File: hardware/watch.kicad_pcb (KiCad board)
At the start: 4 copper layers, 33 x 34 mm, 45 parts, among them J1 Conn_01x02_Male, J2 Conn_01x03_Male, J3 Conn_01x01_Male, J4 Conn_01x03_Male, J5 Conn_01x01_Male, SW1 SW_Push, SW2 SW_Push, U1 KCSA02-105, U10 STP08DP05, U11 KCSA02-105, U12 STP08DP05, U13 KCSA02-105, U2 KCSA02-105, U3 STP08DP05, U4 STP08DP05, U5 STM32L011F4Px, U6 TLV70033_SOT23-5, U7 MCP73831-2-OT, U8 LM66100, U9 LM66100, Y1 32kHz

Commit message: working on hardware rev3
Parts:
- removed C1, C16, C5: 100nF, Capacitor_SMD:C_0603_1608Metric_Pad1.05x0.95mm_HandSolder
- removed J3, J5: Conn_01x01_Male, Connector_PinHeader_2.54mm:PinHeader_1x01_P2.54mm_Vertical
- removed J4: Conn_01x03_Male, Connector_PinHeader_2.54mm:PinHeader_1x03_P2.54mm_Vertical
- added R9: 2k, Resistor_SMD:R_0603_1608Metric_Pad1.05x0.95mm_HandSolder, F.Cu at (169.0, 89.8)
- BT1, C10, C14, C15, C3, C4, C6, C7, C8, C9, R3, R6, R7, R8, U5, U6, U7, Y1: moved to F.Cu
- J1: value Conn_01x02_Male -> USB_C_Receptacle_USB2.0; footprint Connector_PinHeader_2.54mm:PinHeader_1x02_P2.54mm_Vertical -> Connector_USB:USB_C_Receptacle_Palconn_UTC16-G; moved to F.Cu
- J2: value Conn_01x03_Male -> Conn_01x04_Male; footprint Connector_PinHeader_2.54mm:PinHeader_1x03_P2.54mm_Vertical -> Connector_PinHeader_2.54mm:PinHeader_1x04_P2.54mm_Vertical; moved to F.Cu
- R2: value 2k -> 10k
- U10, U4: moved to B.Cu
- U12: value STP08DP05 -> TCPP01-M12; footprint Package_SO:TSSOP-16_4.4x5mm_P0.65mm -> Package_DFN_QFN:QFN-12-1EP_3x3mm_P0.51mm_EP1.45x1.45mm
- U3: value STP08DP05 -> TPS2115A-Q1; footprint Package_SO:TSSOP-16_4.4x5mm_P0.65mm -> watch:TSSOP-8_3x6.4_P0.65mm
- U8, U9: value LM66100 -> STP08DP05; footprint lm66100:LM66100DCKT -> Package_SO:TSSOP-16_4.4x5mm_P0.65mm
- moved R4 50.5 mm to (169.0, 87.3), turned to 0 degrees
- moved BT1 38.3 mm to (190.5, 60.9), turned to 0 degrees
- moved J2 35.1 mm to (144.0, 42.9)
- moved R5 33.7 mm to (177.8, 80.7), turned to 0 degrees
- moved U12 27.1 mm to (127.5, 54.9)
- moved C10 24.6 mm to (155.4, 49.7), turned to 0 degrees
- moved C11 24.2 mm to (136.0, 75.9), turned to 0 degrees
- moved SW1 23.9 mm to (136.0, 72.9)
- moved R8 23.1 mm to (144.9, 47.9), turned to 0 degrees
- moved C4 23.0 mm to (164.5, 49.4)
- moved U1 22.5 mm to (158.3, 62.9)
- moved U13 22.5 mm to (135.8, 62.9)
- moved U10 21.2 mm to (158.3, 62.9), turned to -90 degrees
- moved C6 19.6 mm to (139.0, 49.4), turned to 180 degrees
- moved R2 19.5 mm to (157.5, 54.9), turned to 0 degrees
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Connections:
- U1 pad 1: /S1_E -> /S2_E
- U1 pad 10: /S1_G -> /S2_G
- U1 pad 2: /S1_D -> /S2_D
- U1 pad 4: /S1_C -> /S2_C
- U1 pad 5: /S1_DP -> /S2_DP
- U1 pad 6: /S1_B -> /S2_B
- U1 pad 7: /S1_A -> /S2_A
- U1 pad 9: /S1_F -> /S2_F
- U10 pad 10: /S2_G -> Net-(U10-Pad10)
- U10 pad 11: /S2_A -> Net-(U10-Pad11)
- U10 pad 12: /S2_B -> Net-(U10-Pad12)
- U10 pad 15: Net-(R4-Pad1) -> Net-(R9-Pad1)
- U10 pad 5: /S1_G -> Net-(U10-Pad5)
- U10 pad 6: /S1_F -> Net-(U10-Pad6)
- U10 pad 7: /S1_B -> Net-(U10-Pad7)
- U10 pad 8: /S1_A -> Net-(U10-Pad8)
- U10 pad 9: /S2_F -> Net-(U10-Pad9)
- U11 pad 1: /S3_E -> /S2_E
- U11 pad 10: /S3_G -> /S2_G
- U11 pad 2: /S3_D -> /S2_D
- U11 pad 4: /S3_C -> /S2_C
- U11 pad 5: /S3_DP -> /S2_DP
- U11 pad 6: /S3_B -> /S2_B
- U11 pad 7: /S3_A -> /S2_A
- U11 pad 9: /S3_F -> /S2_F
- U12 pad 1: GND -> Net-(U12-Pad1)
- U12 pad 10: /S4_G -> Net-(U12-Pad10)
- U12 pad 11: /S4_A -> Net-(U12-Pad11)
- U12 pad 12: /S4_B -> Net-(U12-Pad12)
- U12 pad 13: /OE -> Net-(U12-Pad13)
- U12 pad 2: Net-(U10-Pad14) -> Net-(U12-Pad2)
- U12 pad 3: /CLK -> Net-(U12-Pad3)
- U12 pad 4: /LE -> Net-(U12-Pad4)
- U12 pad 5: /S3_G -> Net-(U12-Pad5)
- U12 pad 6: /S3_F -> Net-(U12-Pad6)
- U12 pad 7: /S3_B -> Net-(U12-Pad7)
- U12 pad 8: /S3_A -> Net-(U12-Pad8)
- U12 pad 9: /S4_F -> Net-(U12-Pad9)
- U13 pad 1: /S4_E -> /S2_E
- U13 pad 10: /S4_G -> /S2_G
- U13 pad 2: /S4_D -> /S2_D
- U13 pad 4: /S4_C -> /S2_C
- U13 pad 5: /S4_DP -> /S2_DP
- U13 pad 6: /S4_B -> /S2_B
- U13 pad 7: /S4_A -> /S2_A
- U13 pad 9: /S4_F -> /S2_F
- U3 pad 1: GND -> Net-(U3-Pad1)
- U3 pad 2: Net-(U3-Pad2) -> GND
- U3 pad 3: /CLK -> Net-(U3-Pad3)
- U3 pad 4: /LE -> Net-(R2-Pad1)
- U3 pad 5: /S4_DP -> +5V
- U3 pad 6: /S4_C -> VCC
- U3 pad 7: /S4_E -> +BATT
- U3 pad 8: /S4_D -> GND
- U4 pad 14: Net-(U3-Pad2) -> Net-(U4-Pad14)
- U5 pad 8: /TX -> Net-(U5-Pad8)
- U5 pad 9: /RX -> Net-(U5-Pad9)
- U8 pad 1: +BATT -> GND
- U8 pad 2: GND -> Net-(U4-Pad14)
- U8 pad 3: +5V -> /CLK
- U8 pad 4: (no net) -> /LE
- U8 pad 5: GND -> Net-(U8-Pad5)
- U8 pad 6: VCC -> Net-(U8-Pad6)
- U9 pad 1: +5V -> GND
- U9 pad 2: GND -> Net-(U8-Pad14)
- U9 pad 3: +BATT -> /CLK
- U9 pad 4: (no net) -> /LE
- U9 pad 5: GND -> Net-(U9-Pad5)
- U9 pad 6: VCC -> Net-(U9-Pad6)
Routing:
- net GND: track 85.1 -> 0.00 mm, vias 13 -> 0
- net /OE: track 74.3 -> 0.00 mm, vias 4 -> 0
- net /CLK: track 72.9 -> 0.00 mm, vias 4 -> 0
- net /LE: track 69.2 -> 0.00 mm, vias 4 -> 0
- net +3V3: track 61.6 -> 0.00 mm, vias 7 -> 0
- net Net-(U10-Pad2): track 51.4 -> 0.00 mm, vias 2 -> 0
- net /RX: track 46.1 -> 0.00 mm, vias 1 -> 0
- net /ADC: track 44.1 -> 0.00 mm
- net +BATT: track 42.9 -> 0.00 mm, vias 2 -> 0
- net VCC: track 40.8 -> 0.00 mm, vias 2 -> 0
- net /TX: track 39.9 -> 0.00 mm, vias 1 -> 0
- net /SW1: track 31.8 -> 0.00 mm, vias 1 -> 0
- net +5V: track 29.2 -> 0.00 mm
- net /MDI: track 26.2 -> 0.00 mm, vias 1 -> 0
- net /NRST: track 24.2 -> 0.00 mm
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- removed copper zone on B.Cu, net +3V3
- removed copper zone on In1.Cu, net +3V3
- removed copper zone on B.Cu, net +5V
- removed copper zone on B.Cu, net +BATT
- removed copper zone on B.Cu, net GND
- removed copper zone on In2.Cu, net GND
- removed copper zone on B.Cu, net VCC
- removed copper zone on F.Cu, net VCC
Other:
- board size 33 x 34 mm -> 48 x 34 mm
- net class Default removed
- board text removed: "BAT"
- board text removed: "SWD"
- board text removed: "UART"

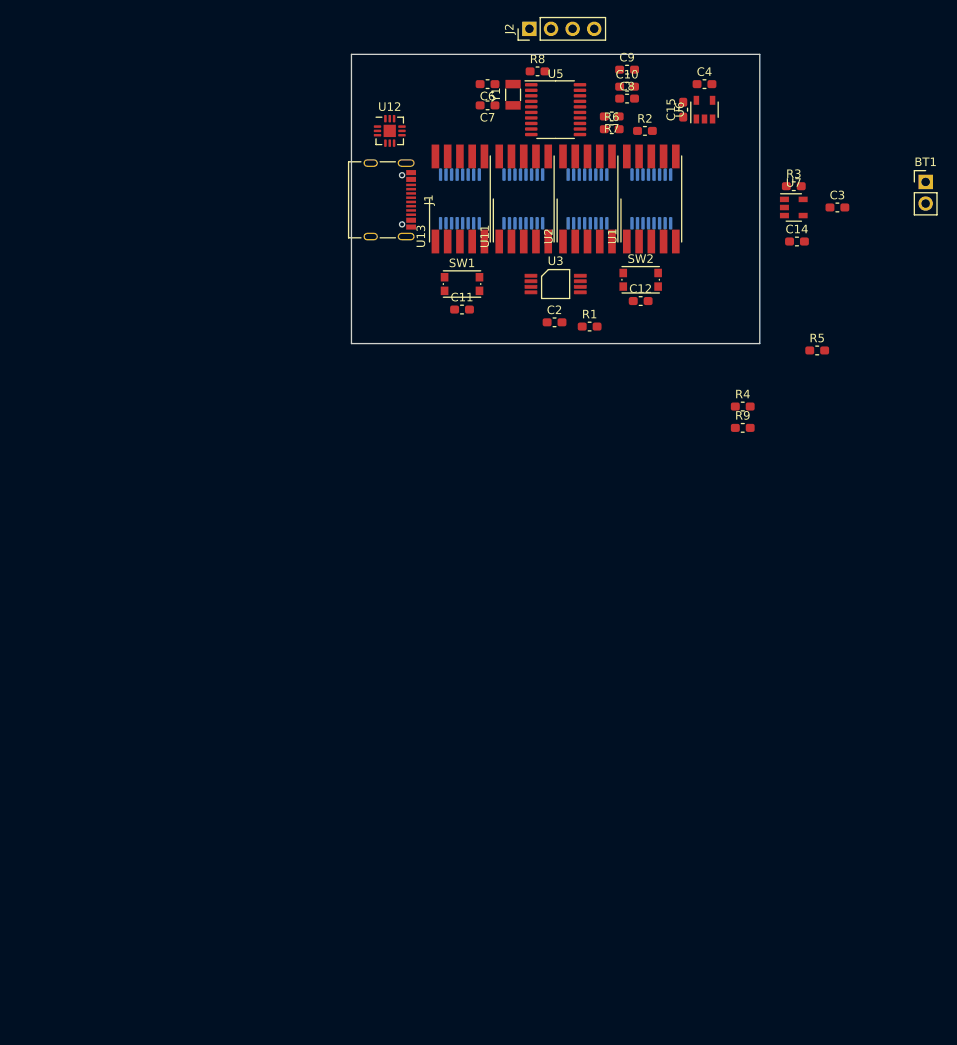
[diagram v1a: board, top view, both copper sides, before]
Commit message: schematic should be done, pcb is next
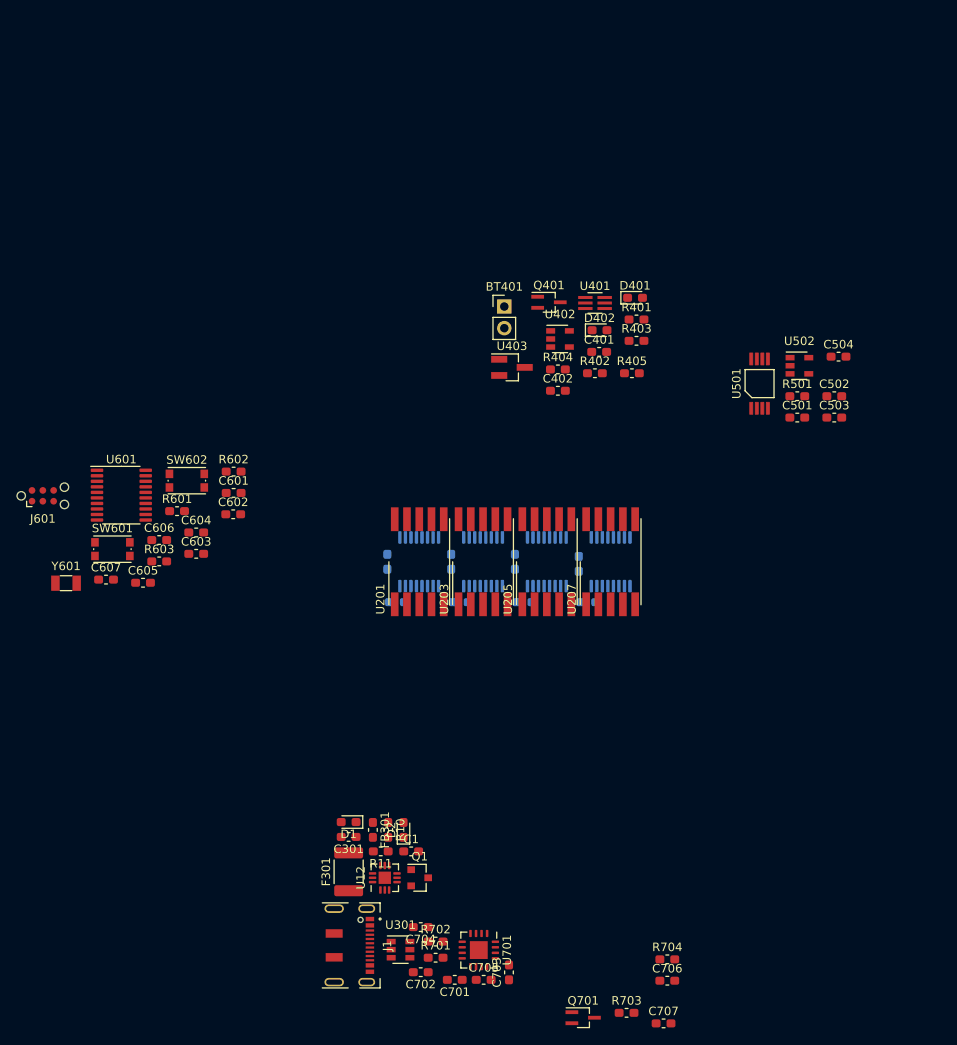
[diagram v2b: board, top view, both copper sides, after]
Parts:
- removed BT1: Battery_Cell, Connector_PinHeader_2.54mm:PinHeader_1x02_P2.54mm_Vertical
- removed C10, C11, C12, C2, C9: 100nF, Capacitor_SMD:C_0603_1608Metric_Pad1.05x0.95mm_HandSolder
- removed C14, C3, C8: 10uF, Capacitor_SMD:C_0603_1608Metric_Pad1.05x0.95mm_HandSolder
- removed C15, C4: 1uF, Capacitor_SMD:C_0603_1608Metric_Pad1.05x0.95mm_HandSolder
- removed C6, C7: 12pF, Capacitor_SMD:C_0603_1608Metric_Pad1.05x0.95mm_HandSolder
- removed J2: Conn_01x04_Male, Connector_PinHeader_2.54mm:PinHeader_1x04_P2.54mm_Vertical
- removed R1, R4, R5, R9: 2k, Resistor_SMD:R_0603_1608Metric_Pad1.05x0.95mm_HandSolder
- removed R2: 10k, Resistor_SMD:R_0603_1608Metric_Pad1.05x0.95mm_HandSolder
- removed R3: 3k9, Resistor_SMD:R_0603_1608Metric_Pad1.05x0.95mm_HandSolder
- removed R6, R7: 47k, Resistor_SMD:R_0603_1608Metric_Pad1.05x0.95mm_HandSolder
- removed R8: 100k, Resistor_SMD:R_0603_1608Metric_Pad1.05x0.95mm_HandSolder
- removed SW1, SW2: SW_Push, Button_Switch_SMD:SW_Push_1P1T_NO_CK_KMR2
- removed U1, U11, U13, U2: KCSA02-105, Display_7Segment:KCSC02-105
- removed U10, U4, U8, U9: STP08DP05, Package_SO:TSSOP-16_4.4x5mm_P0.65mm
- removed U3: TPS2115A-Q1, watch:TSSOP-8_3x6.4_P0.65mm
- removed U5: STM32L011F4Px, Package_SO:TSSOP-20_4.4x6.5mm_P0.65mm
- removed U6: TLV70033_SOT23-5, Package_TO_SOT_SMD:SOT-23-5
- removed U7: MCP73831-2-OT, Package_TO_SOT_SMD:SOT-23-5
- removed Y1: 32kHz, Crystal:Crystal_SMD_3215-2Pin_3.2x1.5mm
- added BT401: Battery_Cell, Connector_PinHeader_2.54mm:PinHeader_1x02_P2.54mm_Vertical, F.Cu at (141.0, 75.5)
- added C1: 100n, Capacitor_SMD:C_0603_1608Metric_Pad1.05x0.95mm_HandSolder, F.Cu at (130.1, 139.6)
- added C201: 100n, Capacitor_SMD:C_0603_1608Metric_Pad1.05x0.95mm_HandSolder, B.Cu at (127.2, 105.5)
- added C202: 100n, Capacitor_SMD:C_0603_1608Metric_Pad1.05x0.95mm_HandSolder, B.Cu at (134.8, 105.5)
- added C203: 100n, Capacitor_SMD:C_0603_1608Metric_Pad1.05x0.95mm_HandSolder, B.Cu at (142.2, 105.5)
- added C204: 100n, Capacitor_SMD:C_0603_1608Metric_Pad1.05x0.95mm_HandSolder, B.Cu at (149.8, 105.8)
- added C301: 10n, Capacitor_SMD:C_0603_1608Metric_Pad1.05x0.95mm_HandSolder, F.Cu at (122.7, 137.8)
- added C401: 10u, Capacitor_SMD:C_0603_1608Metric_Pad1.05x0.95mm_HandSolder, F.Cu at (152.2, 80.8)
- added C402: 10u, Capacitor_SMD:C_0603_1608Metric_Pad1.05x0.95mm_HandSolder, F.Cu at (147.3, 85.4)
- added C501: 100n, Capacitor_SMD:C_0603_1608Metric_Pad1.05x0.95mm_HandSolder, F.Cu at (175.4, 88.5)
- added C502: 100n, Capacitor_SMD:C_0603_1608Metric_Pad1.05x0.95mm_HandSolder, F.Cu at (179.8, 86.0)
- added C503: 1u, Capacitor_SMD:C_0603_1608Metric_Pad1.05x0.95mm_HandSolder, F.Cu at (179.8, 88.5)
- added C504: 1u, Capacitor_SMD:C_0603_1608Metric_Pad1.05x0.95mm_HandSolder, F.Cu at (180.3, 81.4)
- added C601: 12p, Capacitor_SMD:C_0603_1608Metric_Pad1.05x0.95mm_HandSolder, F.Cu at (109.2, 97.4)
- added C602: 12p, Capacitor_SMD:C_0603_1608Metric_Pad1.05x0.95mm_HandSolder, F.Cu at (109.1, 99.9)
- added C603: 100n, Capacitor_SMD:C_0603_1608Metric_Pad1.05x0.95mm_HandSolder, F.Cu at (104.8, 104.6)
- added C604: 100n, Capacitor_SMD:C_0603_1608Metric_Pad1.05x0.95mm_HandSolder, F.Cu at (104.8, 102.1)
- added C605: 10u, Capacitor_SMD:C_0603_1608Metric_Pad1.05x0.95mm_HandSolder, F.Cu at (98.5, 108.0)
- added C606: 100n, Capacitor_SMD:C_0603_1608Metric_Pad1.05x0.95mm_HandSolder, F.Cu at (100.4, 103.0)
- added C607: 100n, Capacitor_SMD:C_0603_1608Metric_Pad1.05x0.95mm_HandSolder, F.Cu at (94.2, 107.6)
- added C701: 100n, Capacitor_SMD:C_0603_1608Metric_Pad1.05x0.95mm_HandSolder, F.Cu at (135.2, 154.7)
- added C702: 47p, Capacitor_SMD:C_0603_1608Metric_Pad1.05x0.95mm_HandSolder, F.Cu at (131.2, 153.8)
- added C703: 4.7u, Capacitor_SMD:C_0603_1608Metric_Pad1.05x0.95mm_HandSolder, F.Cu at (141.6, 153.8)
- added C704: 47p, Capacitor_SMD:C_0603_1608Metric_Pad1.05x0.95mm_HandSolder, F.Cu at (131.2, 148.4)
- added C705: 100n, Capacitor_SMD:C_0603_1608Metric_Pad1.05x0.95mm_HandSolder, F.Cu at (138.6, 154.7)
- added C706: 100n, Capacitor_SMD:C_0603_1608Metric_Pad1.05x0.95mm_HandSolder, F.Cu at (160.2, 154.8)
- added C707: 100n, Capacitor_SMD:C_0603_1608Metric_Pad1.05x0.95mm_HandSolder, F.Cu at (159.7, 159.8)
- added D1: ESDA25P35-1U1M, Diode_SMD:D_0603_1608Metric_Pad1.05x0.95mm_HandSolder, F.Cu at (122.7, 136.1)
- added D2: NSR20F30NXT5G, Diode_SMD:D_0603_1608Metric_Pad1.05x0.95mm_HandSolder, F.Cu at (129.2, 137.0)
- added D401: RED, LED_SMD:LED_0603_1608Metric_Pad1.05x0.95mm_HandSolder, F.Cu at (156.4, 74.5)
- added D402: GREEN, LED_SMD:LED_0603_1608Metric_Pad1.05x0.95mm_HandSolder, F.Cu at (152.2, 78.3)
- added F301: 1812L050/60MR, Fuse:Fuse_1812_4532Metric_Pad1.30x3.40mm_HandSolder, F.Cu at (122.7, 141.9)
- added FB301: 600R@100MHz, Inductor_SMD:L_0603_1608Metric_Pad1.05x0.95mm_HandSolder, F.Cu at (125.5, 137.0)
- added J601: SWD, Connector:Tag-Connect_TC2030-IDC-NL_2x03_P1.27mm_Vertical, F.Cu at (86.8, 97.8)
- added Q1: DMN6140L, Package_TO_SOT_SMD:SOT-23, F.Cu at (131.1, 142.7)
- added Q401: DMP2110UW-7, Package_TO_SOT_SMD:SOT-323_SC-70_Handsoldering, F.Cu at (146.2, 75.0)
- added Q701: DMP2110UW-7, Package_TO_SOT_SMD:SOT-323_SC-70_Handsoldering, F.Cu at (150.3, 159.1)
- added R10: 10k, Resistor_SMD:R_0603_1608Metric_Pad1.05x0.95mm_HandSolder, F.Cu at (127.3, 137.0)
- added R11: 2k7, Resistor_SMD:R_0603_1608Metric_Pad1.05x0.95mm_HandSolder, F.Cu at (126.5, 139.6)
- added R201: 2k, Resistor_SMD:R_0603_1608Metric_Pad1.05x0.95mm_HandSolder, B.Cu at (128.4, 110.2)
- added R202: 2k, Resistor_SMD:R_0603_1608Metric_Pad1.05x0.95mm_HandSolder, B.Cu at (135.9, 110.2)
- added R203: 2k, Resistor_SMD:R_0603_1608Metric_Pad1.05x0.95mm_HandSolder, B.Cu at (143.4, 110.2)
- added R204: 2k, Resistor_SMD:R_0603_1608Metric_Pad1.05x0.95mm_HandSolder, B.Cu at (150.9, 110.2)
- added R401: 10k, Resistor_SMD:R_0603_1608Metric_Pad1.05x0.95mm_HandSolder, F.Cu at (156.5, 77.0)
- added R402: 10k, Resistor_SMD:R_0603_1608Metric_Pad1.05x0.95mm_HandSolder, F.Cu at (151.7, 83.3)
- added R403: R, Resistor_SMD:R_0603_1608Metric_Pad1.05x0.95mm_HandSolder, F.Cu at (156.5, 79.5)
- added R404: 47k, Resistor_SMD:R_0603_1608Metric_Pad1.05x0.95mm_HandSolder, F.Cu at (147.3, 82.9)
- added R405: 47k, Resistor_SMD:R_0603_1608Metric_Pad1.05x0.95mm_HandSolder, F.Cu at (156.0, 83.3)
- added R501: 10k, Resistor_SMD:R_0603_1608Metric_Pad1.05x0.95mm_HandSolder, F.Cu at (175.4, 86.0)
- added R601: R_Small, Resistor_SMD:R_0603_1608Metric_Pad1.05x0.95mm_HandSolder, F.Cu at (102.5, 99.5)
- added R602: 100k, Resistor_SMD:R_0603_1608Metric_Pad1.05x0.95mm_HandSolder, F.Cu at (109.2, 94.9)
- added R603: R_Small, Resistor_SMD:R_0603_1608Metric_Pad1.05x0.95mm_HandSolder, F.Cu at (100.4, 105.5)
- added R701: 27R, Resistor_SMD:R_0603_1608Metric_Pad1.05x0.95mm_HandSolder, F.Cu at (132.9, 152.1)
- added R702: 27R, Resistor_SMD:R_0603_1608Metric_Pad1.05x0.95mm_HandSolder, F.Cu at (132.9, 150.2)
- added R703: 100k, Resistor_SMD:R_0603_1608Metric_Pad1.05x0.95mm_HandSolder, F.Cu at (155.4, 158.5)
- added R704: 1k, Resistor_SMD:R_0603_1608Metric_Pad1.05x0.95mm_HandSolder, F.Cu at (160.2, 152.2)
- added SW601: SW_Push, Button_Switch_SMD:SW_Push_1P1T_NO_CK_KMR2, F.Cu at (94.9, 104.0)
- added SW602: SW_Push, Button_Switch_SMD:SW_Push_1P1T_NO_CK_KMR2, F.Cu at (103.7, 96.0)
- added U201: KCSA02-105, Display_7Segment:KCSC02-105, F.Cu at (131.0, 105.5)
- added U202: STP08DP05, Package_SO:TSSOP-16_4.4x5mm_P0.65mm, B.Cu at (131.0, 105.5)
- added U203: KCSA02-105, Display_7Segment:KCSC02-105, F.Cu at (138.5, 105.5)
- added U204: STP08DP05, Package_SO:TSSOP-16_4.4x5mm_P0.65mm, B.Cu at (138.5, 105.5)
- added U205: KCSA02-105, Display_7Segment:KCSC02-105, F.Cu at (146.0, 105.5)
- added U206: STP08DP05, Package_SO:TSSOP-16_4.4x5mm_P0.65mm, B.Cu at (153.5, 105.5)
- added U207: KCSA02-105, Display_7Segment:KCSC02-105, F.Cu at (153.5, 105.5)
- added U208: STP08DP05, Package_SO:TSSOP-16_4.4x5mm_P0.65mm, B.Cu at (146.0, 105.5)
- added U301: USBLC6-2SC6, Package_TO_SOT_SMD:SOT-23-6, F.Cu at (128.8, 151.1)
- added U401: LM66100, lm66100:LM66100DCKT, F.Cu at (151.7, 75.1)
- added U402: MCP73831-2-OT, Package_TO_SOT_SMD:SOT-23-5, F.Cu at (147.6, 79.3)
- added U403: TLV810E, Package_TO_SOT_SMD:SOT-23_Handsoldering, F.Cu at (141.9, 82.7)
- added U501: TPS2115A-Q1, watch:TSSOP-8_3x6.4_P0.65mm, F.Cu at (171.0, 84.6)
- added U502: TLV70033_SOT23-5, Package_TO_SOT_SMD:SOT-23-5, F.Cu at (175.7, 82.5)
- added U601: STM32L011F4Px, Package_SO:TSSOP-20_4.4x6.5mm_P0.65mm, F.Cu at (96.0, 97.7)
- added U701: FT230XQ, Package_DFN_QFN:QFN-16-1EP_4x4mm_P0.65mm_EP2.1x2.1mm, F.Cu at (138.0, 151.2)
- added Y601: 32kHz, Crystal:Crystal_SMD_3215-2Pin_3.2x1.5mm, F.Cu at (89.5, 108.0)
- J1: value USB_C_Receptacle_USB2.0 -> DX07S016JA1R1500; footprint Connector_USB:USB_C_Receptacle_Palconn_UTC16-G -> watch:DX07S016JA1R1500
- moved J1 87.9 mm to (121.0, 150.6)
- moved U12 87.8 mm to (127.0, 142.7), turned to 90 degrees
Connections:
- net Net-(J1-PadA4) renamed /USB Protection Circuits/VBUS
- J1 pad A1: Net-(J1-PadA1) -> GND
- J1 pad A12: Net-(J1-PadA1) -> GND
- J1 pad A5: Net-(J1-PadA5) -> /USB Protection Circuits/CC1
- J1 pad A6: Net-(J1-PadA6) -> /USB Protection Circuits/D+_IN
- J1 pad A7: Net-(J1-PadA7) -> /USB Protection Circuits/D-_IN
- J1 pad B1: Net-(J1-PadA1) -> GND
- J1 pad B12: Net-(J1-PadA1) -> GND
- J1 pad B5: Net-(J1-PadB5) -> /USB Protection Circuits/CC2
- J1 pad B6: Net-(J1-PadB6) -> /USB Protection Circuits/D+_IN
- J1 pad B7: Net-(J1-PadB7) -> /USB Protection Circuits/D-_IN
- J1 pad S1: Net-(J1-PadS1) -> GND
- U12 pad 1: Net-(U12-Pad1) -> GND
- U12 pad 10: Net-(U12-Pad10) -> GND
- U12 pad 11: Net-(U12-Pad11) -> GND
- U12 pad 12: Net-(U12-Pad12) -> GND
- U12 pad 13: Net-(U12-Pad13) -> GND
- U12 pad 2: Net-(U12-Pad2) -> GND
- U12 pad 3: Net-(U12-Pad3) -> GND
- U12 pad 4: Net-(U12-Pad4) -> /USB Protection Circuits/5V@500mA
- U12 pad 6: Net-(U12-Pad6) -> /USB Protection Circuits/V_BUS_CTRL
- U12 pad 7: Net-(U12-Pad7) -> /USB Protection Circuits/CC1
- U12 pad 9: Net-(U12-Pad9) -> /USB Protection Circuits/CC2
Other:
- board outline removed
- net class Default added: clearance 0.2, trace_width 0.25, via_dia 0.8, via_drill 0.4

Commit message: wip hw
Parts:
- C1, C301: footprint Capacitor_SMD:C_0603_1608Metric_Pad1.05x0.95mm_HandSolder -> Capacitor_SMD:C_0603_1608Metric; moved to B.Cu
- C201, C202, C203, C204, C501, C502, C503, C504, C601, C602, C603, C604, C606, C607, C701, C702, C704, C705, C706, C707: footprint Capacitor_SMD:C_0603_1608Metric_Pad1.05x0.95mm_HandSolder -> Capacitor_SMD:C_0603_1608Metric
- C401, C402, C605, C703: footprint Capacitor_SMD:C_0603_1608Metric_Pad1.05x0.95mm_HandSolder -> Capacitor_SMD:C_0805_2012Metric
- D1, D2: footprint Diode_SMD:D_0603_1608Metric_Pad1.05x0.95mm_HandSolder -> Diode_SMD:D_0603_1608Metric; moved to B.Cu
- D401, D402: footprint LED_SMD:LED_0603_1608Metric_Pad1.05x0.95mm_HandSolder -> LED_SMD:LED_0603_1608Metric
- F301: footprint Fuse:Fuse_1812_4532Metric_Pad1.30x3.40mm_HandSolder -> Fuse:Fuse_1812_4532Metric; moved to B.Cu
- FB301: footprint Inductor_SMD:L_0603_1608Metric_Pad1.05x0.95mm_HandSolder -> Inductor_SMD:L_0603_1608Metric; moved to B.Cu
- Q1, U12: moved to B.Cu
- Q401, Q701: footprint Package_TO_SOT_SMD:SOT-323_SC-70_Handsoldering -> Package_TO_SOT_SMD:SOT-323_SC-70
- R10, R11: footprint Resistor_SMD:R_0603_1608Metric_Pad1.05x0.95mm_HandSolder -> Resistor_SMD:R_0603_1608Metric; moved to B.Cu
- R201, R202, R203, R204, R401, R402, R403, R404, R405, R501, R601, R602, R603, R701, R702, R703, R704: footprint Resistor_SMD:R_0603_1608Metric_Pad1.05x0.95mm_HandSolder -> Resistor_SMD:R_0603_1608Metric
- U401: footprint lm66100:LM66100DCKT -> watch:Sc70-6
- U403: footprint Package_TO_SOT_SMD:SOT-23_Handsoldering -> Package_TO_SOT_SMD:SOT-23
- moved R603 58.9 mm to (159.2, 102.0)
- moved SW602 56.4 mm to (159.2, 105.7), turned to 90 degrees
- moved C604 54.4 mm to (159.2, 100.4)
- moved C607 52.1 mm to (144.2, 92.9)
- moved BT401 49.8 mm to (159.8, 121.6), turned to 180 degrees
- moved Y601 47.5 mm to (133.3, 89.7), turned to 90 degrees
- moved C605 47.0 mm to (144.3, 97.7)
- moved C707 43.7 mm to (146.7, 118.0), turned to 180 degrees
- moved D401 43.5 mm to (151.4, 117.6), turned to 90 degrees
- moved U601 42.8 mm to (138.5, 93.2)
- moved D402 42.5 mm to (151.4, 120.8), turned to 90 degrees
- moved R501 41.9 mm to (144.3, 114.1), turned to 90 degrees
- moved U402 41.7 mm to (154.1, 120.5), turned to 90 degrees
- moved R401 41.2 mm to (149.8, 117.7), turned to 90 degrees
- moved U401 40.2 mm to (155.9, 115.0), turned to 270 degrees
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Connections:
- net /USB Protection Circuits/D+_IN renamed /USB Protection Circuits/IN_D+
- net /USB Protection Circuits/D-_IN renamed /USB Protection Circuits/IN_D-
- net Net-(R701-Pad2) renamed /USB/CHIP_D+
- net Net-(R702-Pad2) renamed /USB/CHIP_D-
- D402 pad 1: GND -> Net-(D402-Pad1)
- D402 pad 2: Net-(D402-Pad2) -> /Battery Charger/STAT
- R402 pad 1: /Battery Charger/STAT -> Net-(D402-Pad1)
- R402 pad 2: Net-(D402-Pad2) -> GND
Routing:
- net GND: track 0.00 -> 190.7 mm, vias 0 -> 1
- net /Display/V_DISP: track 0.00 -> 71.4 mm, vias 0 -> 2
- net +3V3: track 0.00 -> 37.0 mm
- net /USB Protection Circuits/5V@500mA: track 0.00 -> 33.2 mm, vias 0 -> 1
- net Net-(D1-Pad1): track 0.00 -> 25.3 mm
- net /USB Protection Circuits/V_BUS_CTRL: track 0.00 -> 24.8 mm
- net /USB Protection Circuits/CC1: track 0.00 -> 21.7 mm, vias 0 -> 1
- net /USB Protection Circuits/CC2: track 0.00 -> 18.2 mm, vias 0 -> 1
- net Net-(BT401-Pad1): track 0.00 -> 15.0 mm
- net /Power Selection Circuits/5V: track 0.00 -> 13.8 mm
- net Net-(C401-Pad1): track 0.00 -> 13.4 mm
- net Net-(U202-Pad14): track 0.00 -> 12.9 mm
- net Net-(U206-Pad14): track 0.00 -> 12.8 mm
- net Net-(U204-Pad14): track 0.00 -> 12.8 mm
- net /USB Protection Circuits/VBUS: track 0.00 -> 9.58 mm, vias 0 -> 1
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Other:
- board outline added: 39.1 x 36.2 mm
- net class Default: clearance 0.2 -> 0.1
- rule trace_clearance: 0.2 -> 0.1
- rule trace_min: 0.127 -> 0.1
- rule via_min_size: 0.4 -> 0.2
